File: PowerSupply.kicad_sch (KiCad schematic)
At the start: 16 parts, among them Q1 DMP2160UW-7, U1 MIC2288YD5-TR, U3 MIC2288YD5-TR

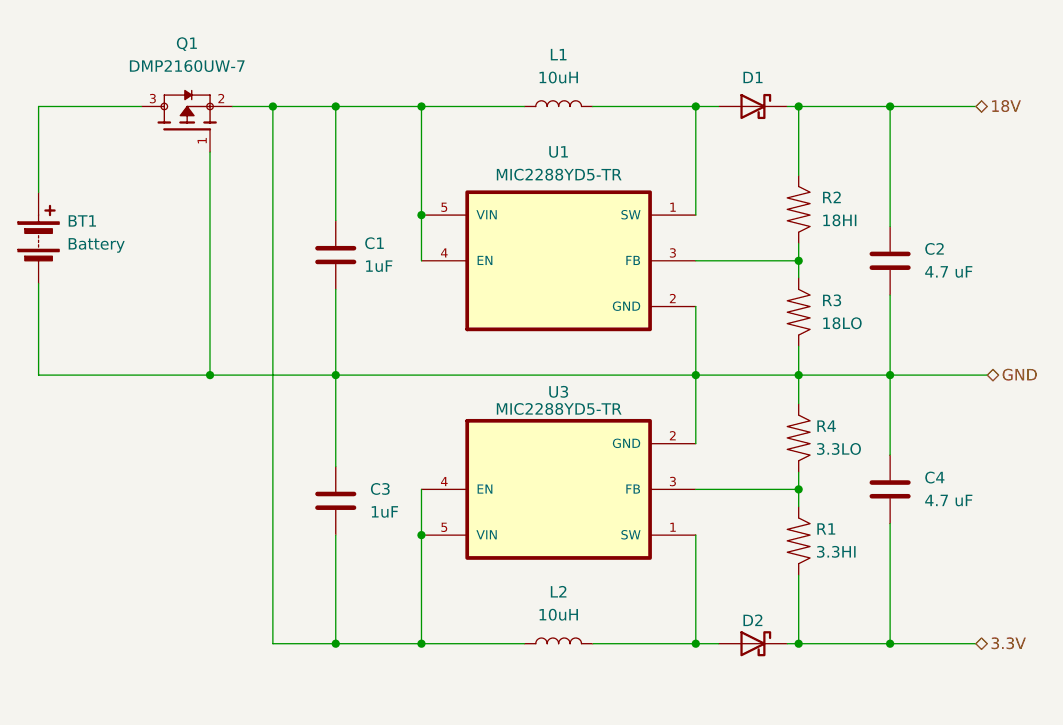
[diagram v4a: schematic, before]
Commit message: Testpoints added to power supply
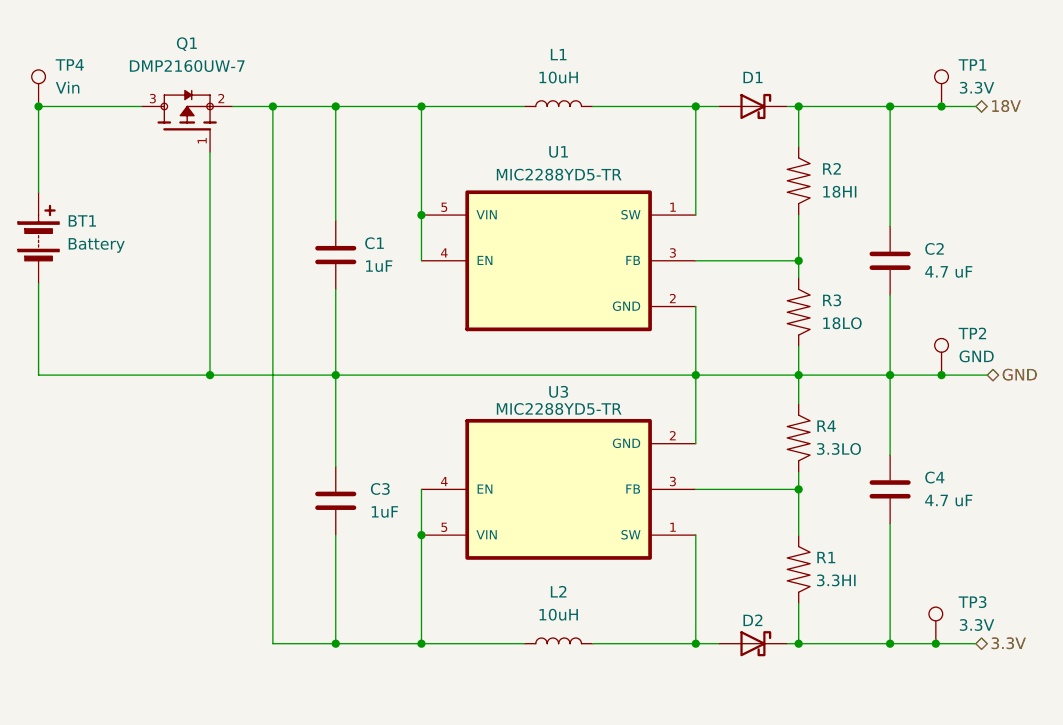
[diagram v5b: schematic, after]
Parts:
- added TP1, TP3: 3.3V, symbol Connector:TestPoint
- added TP2: GND, symbol Connector:TestPoint
- added TP4: Vin, symbol Connector:TestPoint
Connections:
- net 18V: now also TP1.1
- net 3.3V: now also TP3.1
- net GND: now also TP2.1
- net at BT1.1 (+), Q1.3: now also TP4.1
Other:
- moved on the sheet: R1, R2
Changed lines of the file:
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@@
   (junction (at 119.38 116.205) (diameter 0) (color 0 0 0 0)
   )
+  (junction (at 176.53 116.205) (diameter 0) (color 0 0 0 0)
+  )
+  (junction (at 177.165 86.36) (diameter 0) (color 0 0 0 0)
+  )
   (junction (at 161.29 116.205) (diameter 0) (color 0 0 0 0)
   )
@@
   (junction (at 161.29 86.36) (diameter 0) (color 0 0 0 0)
   )
+  (junction (at 177.165 56.515) (diameter 0) (color 0 0 0 0)
+  )
   (junction (at 119.38 68.58) (diameter 0) (color 0 0 0 0)
   )
@@
   (junction (at 149.86 86.36) (diameter 0) (color 0 0 0 0)
   )
+  (junction (at 76.835 56.515) (diameter 0) (color 0 0 0 0)
+  )
   (junction (at 149.86 56.515) (diameter 0) (color 0 0 0 0)
   )
@@
     (stroke (width 0) (type default))
   )
-  (wire (pts (xy 161.29 116.205) (xy 161.29 108.585))
+  (wire (pts (xy 161.29 116.205) (xy 161.29 111.76))
     (stroke (width 0) (type default))
   )
@@
     (stroke (width 0) (type default))
   )
-  (wire (pts (xy 161.29 100.965) (xy 161.29 99.06))
+  (wire (pts (xy 161.29 104.14) (xy 161.29 99.06))
     (stroke (width 0) (type default))
   )
@@
     (stroke (width 0) (type default))
   )
+  (wire (pts (xy 177.165 86.36) (xy 182.245 86.36))
+    (stroke (width 0) (type default))
+  )
   (wire (pts (xy 109.855 56.515) (xy 109.855 69.215))
     (stroke (width 0) (type default))
@@
     (stroke (width 0) (type default))
   )
-  (wire (pts (xy 161.29 71.755) (xy 161.29 73.66))
+  (wire (pts (xy 161.29 68.58) (xy 161.29 73.66))
     (stroke (width 0) (type default))
   )
@@
     (stroke (width 0) (type default))
   )
+  (wire (pts (xy 176.53 116.205) (xy 180.975 116.205))
+    (stroke (width 0) (type default))
+  )
   (wire (pts (xy 119.38 56.515) (xy 130.81 56.515))
     (stroke (width 0) (type default))
@@
     (stroke (width 0) (type default))
   )
-  (wire (pts (xy 171.45 116.205) (xy 180.975 116.205))
+  (wire (pts (xy 171.45 116.205) (xy 176.53 116.205))
+    (stroke (width 0) (type default))
+  )
+  (wire (pts (xy 177.165 56.515) (xy 180.975 56.515))
     (stroke (width 0) (type default))
   )
@@
     (stroke (width 0) (type default))
   )
-  (wire (pts (xy 171.45 56.515) (xy 180.975 56.515))
+  (wire (pts (xy 171.45 56.515) (xy 177.165 56.515))
     (stroke (width 0) (type default))
   )
@@
     (stroke (width 0) (type default))
   )
-  (wire (pts (xy 171.45 86.36) (xy 182.245 86.36))
+  (wire (pts (xy 171.45 86.36) (xy 177.165 86.36))
     (stroke (width 0) (type default))
   )
@@
     (stroke (width 0) (type default))
   )
-  (wire (pts (xy 161.29 56.515) (xy 161.29 64.135))
+  (wire (pts (xy 161.29 56.515) (xy 161.29 60.96))
     (stroke (width 0) (type default))
   )
@@
   (hierarchical_label "3.3V" (shape bidirectional) (at 180.975 116.205 0) (fields_autoplaced)
     (effects (font (size 1.27 1.27)) (justify left))
+  )
+  (symbol (lib_id "Connector:TestPoint") (at 76.835 56.515 0) (unit 1)
+    (in_bom yes) (on_board yes) (dnp no) (fields_autoplaced)
+    (property "Reference" "TP4" (at 78.74 51.943 0)
+      (effects (font (size 1.27 1.27)) (justify left))
+    )
+    (property "Value" "Vin" (at 78.74 54.483 0)
+      (effects (font (size 1.27 1.27)) (justify left))
+    )
+    (property "Footprint" "" (at 81.915 56.515 0)
+      (effects (font (size 1.27 1.27)) hide)
+    )
+    (property "Datasheet" "~" (at 81.915 56.515 0)
+      (effects (font (size 1.27 1.27)) hide)
+    )
+    (pin "1")
+    (instances
+      (project "CatLasers"
+        (path "/b94f5b10-ee0c-4425-b025-e3a8bb3cc7b0/af549741-ba89-4808-a98f-faa5cfb79fa3"
+          (reference "TP4") (unit 1)
+        )
+      )
+    )
   )
   (symbol (lib_id "Hestres_Standard_Lib:D_Schottky") (at 156.21 56.515 0) (mirror y) (unit 1)
@@
     )
   )
-  (symbol (lib_id "Hestres_Standard_Lib:R") (at 161.29 104.775 0) (unit 1)
-    (in_bom yes) (on_board yes) (dnp no)
-    (property "Reference" "R1" (at 163.195 103.505 0)
-      (effects (font (size 1.27 1.27)) (justify left))
-    )
-    (property "Value" "3.3HI" (at 163.195 106.045 0)
-      (effects (font (size 1.27 1.27)) (justify left))
-    )
-    (property "Footprint" "Resistor_SMD:R_0805_2012Metric" (at 159.512 104.775 90)
-      (effects (font (size 1.27 1.27)) hide)
-    )
-    (property "Datasheet" "~" (at 161.29 104.775 0)
+  (symbol (lib_id "Hestres_Standard_Lib:R") (at 161.29 107.95 0) (unit 1)
+    (in_bom yes) (on_board yes) (dnp no)
+    (property "Reference" "R1" (at 163.195 106.68 0)
+      (effects (font (size 1.27 1.27)) (justify left))
+    )
+    (property "Value" "3.3HI" (at 163.195 109.22 0)
+      (effects (font (size 1.27 1.27)) (justify left))
+    )
+    (property "Footprint" "Resistor_SMD:R_0805_2012Metric" (at 159.512 107.95 90)
+      (effects (font (size 1.27 1.27)) hide)
+    )
+    (property "Datasheet" "~" (at 161.29 107.95 0)
       (effects (font (size 1.27 1.27)) hide)
     )
@@
     )
   )
-  (symbol (lib_id "Hestres_Standard_Lib:R") (at 161.29 67.945 0) (unit 1)
+  (symbol (lib_id "Hestres_Standard_Lib:R") (at 161.29 64.77 0) (unit 1)
     (in_bom yes) (on_board yes) (dnp no) (fields_autoplaced)
-    (property "Reference" "R2" (at 163.83 66.675 0)
-      (effects (font (size 1.27 1.27)) (justify left))
-    )
-    (property "Value" "18HI" (at 163.83 69.215 0)
-      (effects (font (size 1.27 1.27)) (justify left))
-    )
-    (property "Footprint" "Resistor_SMD:R_0805_2012Metric" (at 159.512 67.945 90)
-      (effects (font (size 1.27 1.27)) hide)
-    )
-    (property "Datasheet" "~" (at 161.29 67.945 0)
+    (property "Reference" "R2" (at 163.83 63.5 0)
+      (effects (font (size 1.27 1.27)) (justify left))
+    )
+    (property "Value" "18HI" (at 163.83 66.04 0)
+      (effects (font (size 1.27 1.27)) (justify left))
+    )
+    (property "Footprint" "Resistor_SMD:R_0805_2012Metric" (at 159.512 64.77 90)
+      (effects (font (size 1.27 1.27)) hide)
+    )
+    (property "Datasheet" "~" (at 161.29 64.77 0)
       (effects (font (size 1.27 1.27)) hide)
     )
@@
         (path "/b94f5b10-ee0c-4425-b025-e3a8bb3cc7b0/af549741-ba89-4808-a98f-faa5cfb79fa3"
           (reference "L2") (unit 1)
+        )
+      )
+    )
+  )
+  (symbol (lib_id "Connector:TestPoint") (at 176.53 116.205 0) (unit 1)
+    (in_bom yes) (on_board yes) (dnp no) (fields_autoplaced)
+    (property "Reference" "TP3" (at 179.07 111.633 0)
+      (effects (font (size 1.27 1.27)) (justify left))
+    )
+    (property "Value" "3.3V" (at 179.07 114.173 0)
+      (effects (font (size 1.27 1.27)) (justify left))
+    )
+    (property "Footprint" "" (at 181.61 116.205 0)
+      (effects (font (size 1.27 1.27)) hide)
+    )
+    (property "Datasheet" "~" (at 181.61 116.205 0)
+      (effects (font (size 1.27 1.27)) hide)
+    )
+    (pin "1")
+    (instances
+      (project "CatLasers"
+        (path "/b94f5b10-ee0c-4425-b025-e3a8bb3cc7b0/af549741-ba89-4808-a98f-faa5cfb79fa3"
+          (reference "TP3") (unit 1)
         )
       )
@@
     )
   )
+  (symbol (lib_id "Connector:TestPoint") (at 177.165 86.36 0) (unit 1)
+    (in_bom yes) (on_board yes) (dnp no)
+    (property "Reference" "TP2" (at 179.07 81.788 0)
+      (effects (font (size 1.27 1.27)) (justify left))
+    )
+    (property "Value" "GND" (at 179.07 84.328 0)
+      (effects (font (size 1.27 1.27)) (justify left))
+    )
+    (property "Footprint" "" (at 182.245 86.36 0)
+      (effects (font (size 1.27 1.27)) hide)
+    )
+    (property "Datasheet" "~" (at 182.245 86.36 0)
+      (effects (font (size 1.27 1.27)) hide)
+    )
+    (pin "1")
+    (instances
+      (project "CatLasers"
+        (path "/b94f5b10-ee0c-4425-b025-e3a8bb3cc7b0/af549741-ba89-4808-a98f-faa5cfb79fa3"
+          (reference "TP2") (unit 1)
+        )
+      )
+    )
+  )
   (symbol (lib_id "ProjPMOS:DMP2160UW-7") (at 93.345 59.055 270) (mirror x) (unit 1)
     (in_bom yes) (on_board yes) (dnp no) (fields_autoplaced)
@@
         )
       )
+    )
+  )
+  (symbol (lib_id "Connector:TestPoint") (at 177.165 56.515 0) (unit 1)
+    (in_bom yes) (on_board yes) (dnp no)
+    (property "Reference" "TP1" (at 179.07 51.943 0)
+      (effects (font (size 1.27 1.27)) (justify left))
+    )
+    (property "Value" "3.3V" (at 179.07 54.483 0)
+      (effects (font (size 1.27 1.27)) (justify left))
+    )
+    (property "Footprint" "" (at 182.245 56.515 0)
+      (effects (font (size 1.27 1.27)) hide)
+    )
+    (property "Datasheet" "~" (at 182.245 56.515 0)
+      (effects (font (size 1.27 1.27)) hide)
+    )
+    (pin "1")
+    (instances
+      (project "CatLasers"
+        (path "/b94f5b10-ee0c-4425-b025-e3a8bb3cc7b0/af549741-ba89-4808-a98f-faa5cfb79fa3"
+          (reference "TP1") (unit 1)
+        )
+      )

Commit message: Some cleanup
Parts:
- TP1: value 3.3V -> 18V
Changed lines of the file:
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@@
       (effects (font (size 1.27 1.27)) (justify left))
     )
-    (property "Value" "3.3V" (at 179.07 54.483 0)
+    (property "Value" "18V" (at 179.07 54.483 0)
       (effects (font (size 1.27 1.27)) (justify left))
     )

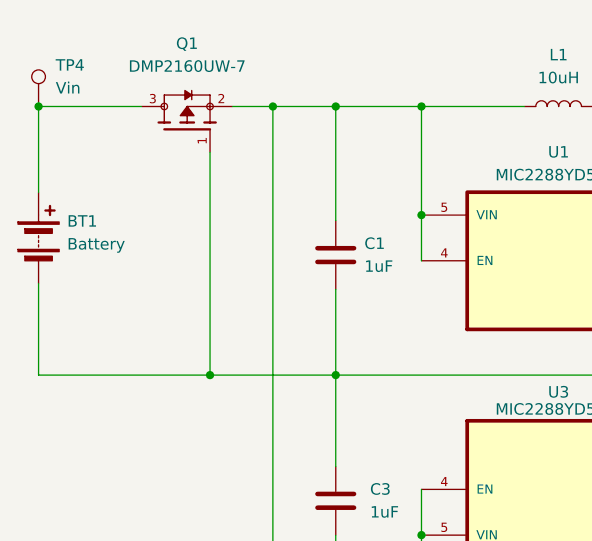
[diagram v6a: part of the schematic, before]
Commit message: Corrected power supply PMOS
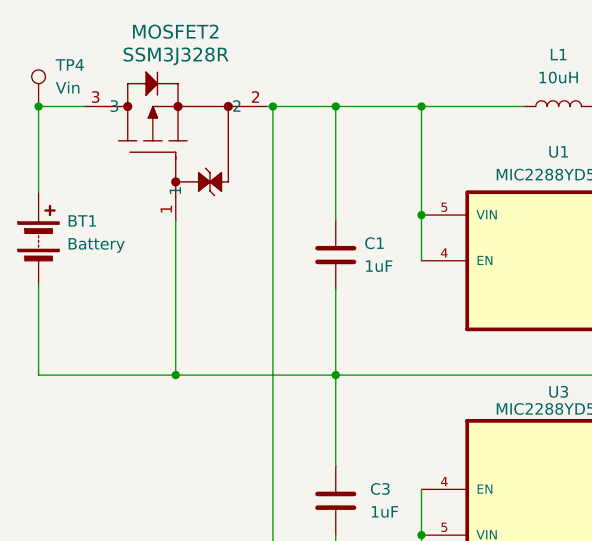
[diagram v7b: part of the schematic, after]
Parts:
- removed Q1: DMP2160UW-7, DMP2160UW-7:TRANS_DMP2160UW-7, symbol ProjPMOS:DMP2160UW-7
- added MOSFET2: SSM3J328R, SOT-23F_TOS, symbol ProjPMOS_LV:SSM3J328R
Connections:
- net GND: now also MOSFET2.1
- net at BT1.1 (+), TP4.1: now also MOSFET2.3
- net at C1.1, C3.2, L1.1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: now also MOSFET2.2
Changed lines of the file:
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@@
   (junction (at 161.29 99.06) (diameter 0) (color 0 0 0 0)
   )
-  (junction (at 95.885 86.36) (diameter 0) (color 0 0 0 0)
-  )
   (junction (at 109.855 56.515) (diameter 0) (color 0 0 0 0)
   )
   (junction (at 119.38 104.14) (diameter 0) (color 0 0 0 0)
   )
+  (junction (at 92.075 86.36) (diameter 0) (color 0 0 0 0)
+  )
   (junction (at 119.38 116.205) (diameter 0) (color 0 0 0 0)
   )
@@
   (junction (at 171.45 86.36) (diameter 0) (color 0 0 0 0)
   )
-  (wire (pts (xy 76.835 56.515) (xy 88.265 56.515))
+  (wire (pts (xy 76.835 56.515) (xy 81.915 56.515))
     (stroke (width 0) (type default))
   )
@@
     (stroke (width 0) (type default))
   )
-  (wire (pts (xy 76.835 86.36) (xy 95.885 86.36))
+  (wire (pts (xy 76.835 86.36) (xy 92.075 86.36))
     (stroke (width 0) (type default))
   )
@@
     (stroke (width 0) (type default))
   )
+  (wire (pts (xy 102.235 56.515) (xy 102.87 56.515))
+    (stroke (width 0) (type default))
+  )
   (wire (pts (xy 119.38 56.515) (xy 130.81 56.515))
     (stroke (width 0) (type default))
@@
     (stroke (width 0) (type default))
   )
-  (wire (pts (xy 95.885 86.36) (xy 109.855 86.36))
+  (wire (pts (xy 92.075 86.36) (xy 109.855 86.36))
     (stroke (width 0) (type default))
   )
@@
     (stroke (width 0) (type default))
   )
-  (wire (pts (xy 95.885 61.595) (xy 95.885 86.36))
-    (stroke (width 0) (type default))
-  )
-  (wire (pts (xy 98.425 56.515) (xy 102.87 56.515))
+  (wire (pts (xy 92.075 69.215) (xy 92.075 86.36))
     (stroke (width 0) (type default))
   )
@@
     )
   )
-  (symbol (lib_id "ProjPMOS:DMP2160UW-7") (at 93.345 59.055 270) (mirror x) (unit 1)
-    (in_bom yes) (on_board yes) (dnp no) (fields_autoplaced)
-    (property "Reference" "Q1" (at 93.345 49.53 90)
-      (effects (font (size 1.27 1.27)))
-    )
-    (property "Value" "DMP2160UW-7" (at 93.345 52.07 90)
-      (effects (font (size 1.27 1.27)))
-    )
-    (property "Footprint" "DMP2160UW-7:TRANS_DMP2160UW-7" (at 93.345 59.055 0)
-      (effects (font (size 1.27 1.27)) (justify bottom) hide)
-    )
-    (property "Datasheet" "" (at 93.345 59.055 0)
-      (effects (font (size 1.27 1.27)) hide)
-    )
-    (property "DigiKey_Part_Number" "DMP2160UWDITR-ND" (at 93.345 59.055 0)
-      (effects (font (size 1.27 1.27)) (justify bottom) hide)
-    )
-    (property "MF" "Diodes Inc." (at 93.345 59.055 0)
-      (effects (font (size 1.27 1.27)) (justify bottom) hide)
-    )
-    (property "MAXIMUM_PACKAGE_HEIGHT" "1.1 mm" (at 93.345 59.055 0)
-      (effects (font (size 1.27 1.27)) (justify bottom) hide)
-    )
-    (property "Package" "SOT-323 Diodes Inc." (at 93.345 59.055 0)
-      (effects (font (size 1.27 1.27)) (justify bottom) hide)
-    )
-    (property "Check_prices" "https://www.snapeda.com/parts/DMP2160UW-7/Diodes+Inc./view-part/?ref=eda" (at 93.345 59.055 0)
-      (effects (font (size 1.27 1.27)) (justify bottom) hide)
-    )
-    (property "STANDARD" "Manufacturer Recommendations" (at 93.345 59.055 0)
-      (effects (font (size 1.27 1.27)) (justify bottom) hide)
-    )
-    (property "PARTREV" "6-3" (at 93.345 59.055 0)
-      (effects (font (size 1.27 1.27)) (justify bottom) hide)
-    )
-    (property "SnapEDA_Link" "https://www.snapeda.com/parts/DMP2160UW-7/Diodes+Inc./view-part/?ref=snap" (at 93.345 59.055 0)
-      (effects (font (size 1.27 1.27)) (justify bottom) hide)
-    )
-    (property "MP" "DMP2160UW-7" (at 93.345 59.055 0)
-      (effects (font (size 1.27 1.27)) (justify bottom) hide)
-    )
-    (property "Purchase-URL" "https://www.snapeda.com/api/url_track_click_mouser/?unipart_id=284587&manufacturer=Diodes Inc.&part_name=DMP2160UW-7&search_term=None" (at 93.345 59.055 0)
-      (effects (font (size 1.27 1.27)) (justify bottom) hide)
-    )
-    (property "Description" "\nMOSFET P-Channel 20V 1.5A SOT323, DMP Series | Diodes Inc DMP2160UW-7\n" (at 93.345 59.055 0)
-      (effects (font (size 1.27 1.27)) (justify bottom) hide)
-    )
-    (property "MANUFACTURER" "Diodes Inc." (at 93.345 59.055 0)
-      (effects (font (size 1.27 1.27)) (justify bottom) hide)
-    )
-    (pin "1")
-    (pin "2")
-    (pin "3")
-    (instances
-      (project "CatLasers"
-        (path "/b94f5b10-ee0c-4425-b025-e3a8bb3cc7b0/af549741-ba89-4808-a98f-faa5cfb79fa3"
-          (reference "Q1") (unit 1)
-        )
-      )
-    )
-  )
   (symbol (lib_id "Connector:TestPoint") (at 177.165 56.515 0) (unit 1)
     (in_bom yes) (on_board yes) (dnp no)
@@
         )
       )
+    )
+  )
+  (symbol (lib_id "ProjPMOS_LV:SSM3J328R") (at 84.455 66.675 90) (unit 1)
+    (in_bom yes) (on_board yes) (dnp no) (fields_autoplaced)
+    (property "Reference" "MOSFET2" (at 92.075 48.26 90)
+      (effects (font (size 1.524 1.524)))
+    )
+    (property "Value" "SSM3J328R" (at 92.075 50.8 90)
+      (effects (font (size 1.524 1.524)))
+    )
+    (property "Footprint" "SOT-23F_TOS" (at 84.455 66.675 0)
+      (effects (font (size 1.27 1.27) italic) hide)
+    )
+    (property "Datasheet" "SSM3J328R" (at 84.455 66.675 0)
+      (effects (font (size 1.27 1.27) italic) hide)
+    )
+    (pin "1")
+    (pin "2")
+    (pin "3")
+    (instances
+      (project "CatLasers"
+        (path "/b94f5b10-ee0c-4425-b025-e3a8bb3cc7b0/af549741-ba89-4808-a98f-faa5cfb79fa3"
+          (reference "MOSFET2") (unit 1)
+        )
+      )

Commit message: Remaining Footprints Assigned
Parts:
- BT1: footprint (none) -> Connector_PinHeader_2.54mm:PinHeader_1x02_P2.54mm_Vertical
- D1, D2: footprint (none) -> Proj:SODFL3618X110N
- MOSFET2: footprint SOT-23F_TOS -> Proj:SOT-23F_TOS
- TP1, TP2, TP3, TP4: footprint (none) -> Proj:TestPoint_KEYSTONE_5019
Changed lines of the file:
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@@
       (effects (font (size 1.27 1.27)) (justify left))
     )
-    (property "Footprint" "" (at 81.915 56.515 0)
+    (property "Footprint" "Proj:TestPoint_KEYSTONE_5019" (at 81.915 56.515 0)
       (effects (font (size 1.27 1.27)) hide)
     )
@@
       (effects (font (size 1.27 1.27)) hide)
     )
-    (property "Footprint" "" (at 156.21 56.515 0)
+    (property "Footprint" "Proj:SODFL3618X110N" (at 156.21 56.515 0)
       (effects (font (size 1.27 1.27)) hide)
     )
@@
       (effects (font (size 1.27 1.27)) (justify left))
     )
-    (property "Footprint" "" (at 181.61 116.205 0)
+    (property "Footprint" "Proj:TestPoint_KEYSTONE_5019" (at 181.61 116.205 0)
       (effects (font (size 1.27 1.27)) hide)
     )
@@
       (effects (font (size 1.27 1.27)) (justify left))
     )
-    (property "Footprint" "" (at 182.245 86.36 0)
+    (property "Footprint" "Proj:TestPoint_KEYSTONE_5019" (at 182.245 86.36 0)
       (effects (font (size 1.27 1.27)) hide)
     )
@@
       (effects (font (size 1.27 1.27)) (justify left))
     )
-    (property "Footprint" "" (at 182.245 56.515 0)
+    (property "Footprint" "Proj:TestPoint_KEYSTONE_5019" (at 182.245 56.515 0)
       (effects (font (size 1.27 1.27)) hide)
     )
@@
       (effects (font (size 1.27 1.27)) (justify left))
     )
-    (property "Footprint" "" (at 76.835 69.596 90)
+    (property "Footprint" "Connector_PinHeader_2.54mm:PinHeader_1x02_P2.54mm_Vertical" (at 76.835 69.596 90)
       (effects (font (size 1.27 1.27)) hide)
     )
@@
       (effects (font (size 1.524 1.524)))
     )
-    (property "Footprint" "SOT-23F_TOS" (at 84.455 66.675 0)
+    (property "Footprint" "Proj:SOT-23F_TOS" (at 84.455 66.675 0)
       (effects (font (size 1.27 1.27) italic) hide)
     )
@@
       (effects (font (size 1.27 1.27)) hide)
     )
-    (property "Footprint" "" (at 156.21 116.205 0)
-      (effects (font (size 1.27 1.27)) hide)
-    )
+    (property "Footprint" "Proj:SODFL3618X110N" (at 156.21 116.205 0)
+      (effects (font (size 1.27 1.27)) hide)
+    )
